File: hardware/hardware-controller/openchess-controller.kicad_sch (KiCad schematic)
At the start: 24 parts, among them J1 Conn_02x13, J2 USB_C_Receptacle_USB2.0_16P, J3 Conn_01x10, U1 AP2112K-3.3, U2 ESP32-DevKitC, U3 74AHCT125

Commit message: Add new mechanical and power symbols for schematic integration
- Introduced new symbols: TestPoint, Fiducial, MountingHole, +3V3, and GND.
- Each symbol includes properties for reference, value, footprint, datasheet, description, keywords, and filters.
- Implemented a Python script to merge test/mech snippets into the main schematic, ensuring backup and validation of parens.
- The script adds missing symbol definitions and integrates component instances, labels, wires, and power ports.
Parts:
- removed C3, C4: 1µF, symbol Device:C
- removed J2: USB_C_Receptacle_USB2.0_16P, Connector_USB:USB_C_Receptacle_GCT_USB4085, symbol Connector:USB_C_Receptacle_USB2.0_16P
- removed R10, R9: 5.1k, symbol Device:R
- removed U1: AP2112K-3.3, Package_TO_SOT_SMD:SOT-23-5, symbol Regulator_Linear:AP2112K-3.3
- added BT1: LiPo 1S 3.7V (protected), symbol Device:Battery_Cell
- added C11, C12: 100nF, Capacitor_SMD:C_0603_1608Metric, symbol Device:C
- added D2: SS14 (or BAT60A), Diode_SMD:D_SMA, symbol Device:D_Schottky
- added FID1, FID2, FID3: Fiducial, Fiducial:Fiducial_1mm_Mask2mm, symbol Mechanical:Fiducial
- added M1: Lipo Rider Plus, LipoRiderPlus:MODULE_106990290, symbol Connector_Generic:Conn_01x08
- added MH1, MH2, MH3, MH4: M3, MountingHole:MountingHole_3.2mm_M3, symbol Mechanical:MountingHole
- added R14: 220k, Resistor_SMD:R_0603_1608Metric, symbol Device:R
- added R15: 100k, Resistor_SMD:R_0603_1608Metric, symbol Device:R
- added TP1, TP10, TP11, TP12, TP13, TP14, TP15, TP16, TP17, TP18, TP19, TP2, TP20, TP21, TP22, TP3, TP4, TP5, TP6, TP7, TP8, TP9: TestPoint, TestPoint:TestPoint_Pad_D1.5mm, symbol Connector:TestPoint
- added U6: TBD62783A, Package_DIP:DIP-18_W7.62mm, symbol Transistor_Array:TBD62783A
- C1, C2, C5: footprint (none) -> Capacitor_SMD:C_0805_2012Metric
- J1: footprint (none) -> Connector_PinHeader_2.54mm:PinHeader_2x13_P2.54mm_Vertical
- J3: value Conn_01x10 -> J_PANEL XH-10
- R1, R2, R3, R4, R5, R6, R7, R8: footprint (none) -> Resistor_SMD:R_0805_2012Metric
- R11: value R -> 33Ω; footprint (none) -> Resistor_SMD:R_0603_1608Metric
- R36, R37: footprint (none) -> Resistor_SMD:R_0603_1608Metric
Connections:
- net +3.3V: now also M1.1 (Pin_1), TP2.1
- net +5V_LED: now also U3.14 (VCC), C11.1, D2.2 (A), M1.4 (Pin_4), TP1.1, U6.9 (VCC)
- net CA_PWR: now also TP15.1, U6.18 (O1)
- net CB_PWR: now also TP16.1, U6.17 (O2)
- net CC_PWR: now also TP17.1, U6.16 (O3)
- net CD_PWR: now also TP18.1, U6.15 (O4)
- net CE_PWR: now also TP19.1, U6.14 (O5)
- net CF_PWR: now also TP20.1, U6.13 (O6)
- net CG_PWR: now also TP21.1, U6.12 (O7)
- net CH_PWR: now also TP22.1, U6.11 (O8)
- net COL_DRV_A: now also U6.1 (I1)
- net COL_DRV_B: now also U6.2 (I2)
- net COL_DRV_C: now also U6.3 (I3)
- net COL_DRV_D: now also U6.4 (I4)
- net COL_DRV_E: now also U6.5 (I5)
- net COL_DRV_F: now also U6.6 (I6)
- net COL_DRV_G: now also U6.7 (I7)
- net COL_DRV_H: now also U6.8 (I8)
- net GND: now also U3.7 (GND), C11.2, C12.2, M1.3 (Pin_3), M1.5 (Pin_5), M1.7 (Pin_7), R15.2, TP3.1, U6.10 (GND)
- net LED_DATA: now also TP4.1
- net LED_DATA_5V: now also TP5.1
- net PANEL_SPARE: now also J3.8 (Pin_8); no longer J3.9 (Pin_9)
- net S0: now also TP7.1; no longer U2.27 (GPIO16)
- net S1: now also U2.27 (GPIO16), TP8.1
- net S2: now also TP9.1
- net S3: now also TP10.1
- net S4: now also TP11.1
- net S5: now also TP12.1
- net S6: now also TP13.1
- net S7: now also TP14.1
- net at U2.19 (5V): now also D2.1 (K)
- net VBAT_MON: now reaches U2.5 (VDET_1/GPIO34/ADC1_CH6)
- net VBAT_MON: now also C12.1, R14.2, R15.1, TP6.1
- net BTN_RESET: no longer names the net of U2.2 (CHIP_PU)
- net BTN_RESET: no longer J3.8 (Pin_8)
- net LED_BATT_N renamed BTN_SELECT
- net LED_CONN_N renamed I2C_SCL
- net LED_PWR_N renamed I2C_SDA
- new net BAT: M1.6 (Pin_6), R14.1
- new net PANEL_SPARE2: J3.9 (Pin_9)
- no-connect marks 20 -> 17
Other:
- note added: "J3 JST XH 10-pin / → OLED + 3 panel-mount buttons / via flying-lead harness (no panel PCB)"
- note added: "M1 Lipo Rider Plus (USB-C) / → +5V_LED + +3V3 rails / LiPo battery via M1 JST / D2 Schottky → DevKit pin 19"
- note added: "R1..R8 — 10k S0..S7 pulled to +3.3V on controller Hall outputs are open-collector"
- note added: "U2 ESP32-DevKitC v4 / UART0 (GPIO1/3) repurposed as I²C / Flash pins + extras → NC"
- note added: "U3 74AHCT125 quad buffer / Gate A active, B/C/D tied off / R11 33Ω series on output"
- note added: "U6 TBD62783A 8-channel / high-side P-MOSFET driver IC / COL_DRV_A..H → CA..CH_PWR"
- note removed: "CA_PWR..CH_PWR switched 5V column rails Implementation pending: direct GPIO vs 74HC595 + transistors"
- note removed: "Cable-mounted side controls Status LEDs and buttons live off-board Pinout pending"
- note removed: "ESP32 data -> 5V WS2812 data Target net: LED_DATA_5V Part choice pending"
- note removed: "ESP32 module/devkit placeholder GPIO assignment to be locked before placement +3V3 logic rail"
- note removed: "R1..R8 — 10k S0..S7 pulled to +3V3 on controller Hall outputs are open-collector"
- note removed: "USB-C 5V → +5V_LED rail +3V3 LDO (AP2112K-3.3, 600 mA) No battery on prototype #1"
- moved on the sheet: C1, C2, C5, J3, R11, R36, R37, U2, U3A, U3B, U3C, U3D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

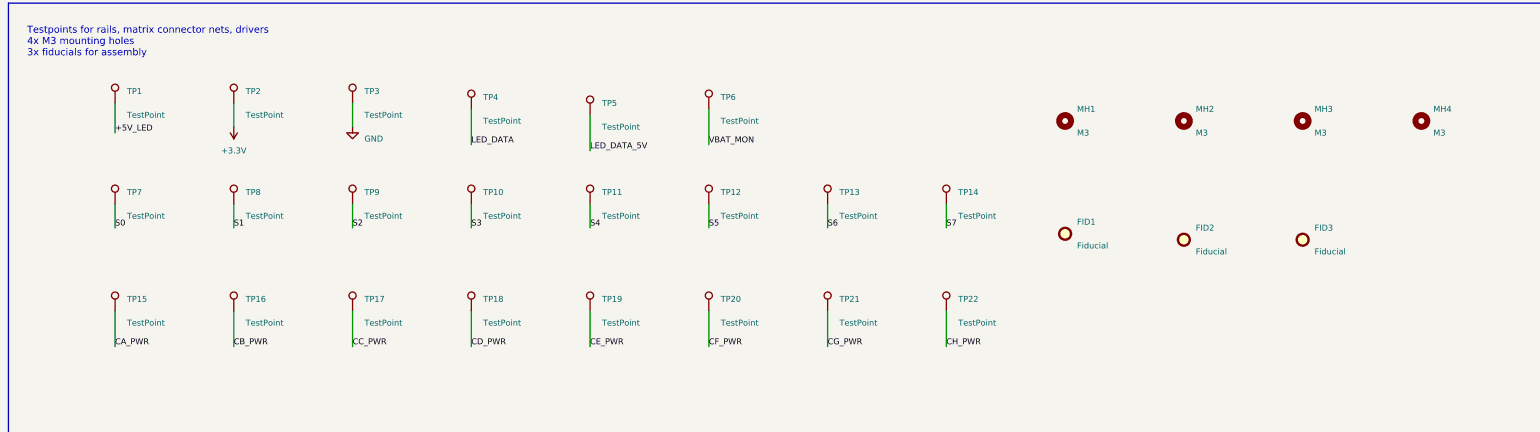
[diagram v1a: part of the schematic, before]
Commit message: Add PCB layout and schematic guides for OpenChess controller
- Introduced `controller-PCB_LAYOUT_GUIDE.planning.md` detailing PCB layout constraints, component placement zones, net classes, routing priorities, and mechanical verification for the OpenChess controller.
- Added `controller-SCHEMATIC_GUIDE.planning.md` providing a comprehensive schematic specification, including reference designators, net lists, component details, and validation rules for the OpenChess controller PCB.
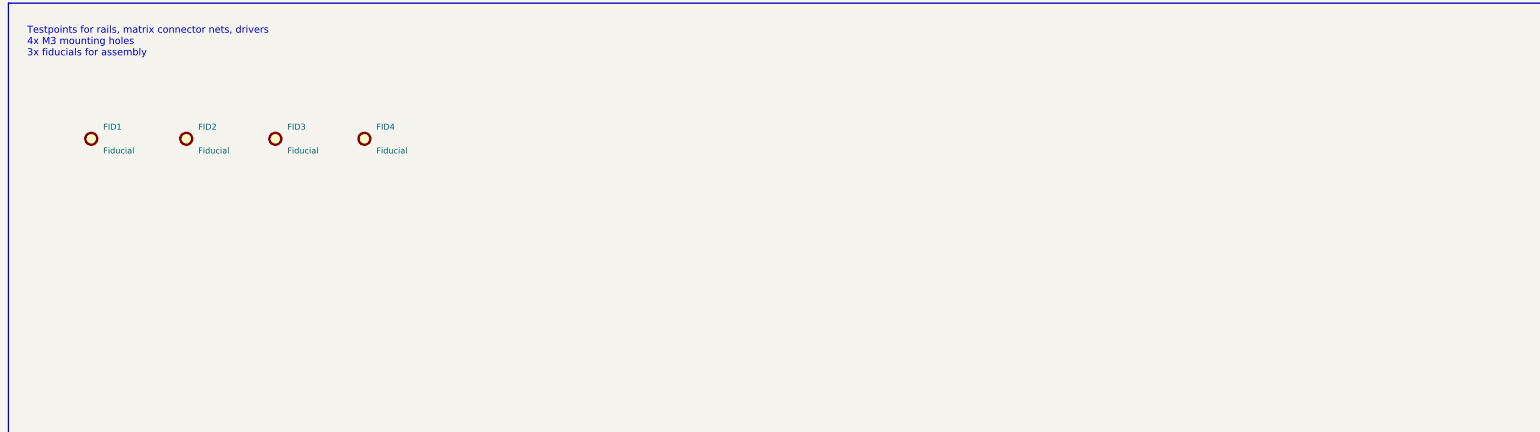
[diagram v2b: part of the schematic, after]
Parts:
- removed MH1, MH2, MH3, MH4: M3, MountingHole:MountingHole_3.2mm_M3, symbol Mechanical:MountingHole
- removed TP1, TP10, TP11, TP12, TP13, TP14, TP15, TP16, TP17, TP18, TP19, TP2, TP20, TP21, TP22, TP3, TP4, TP5, TP6, TP7, TP8, TP9: TestPoint, TestPoint:TestPoint_Pad_D1.5mm, symbol Connector:TestPoint
- added FID4: Fiducial, Fiducial:Fiducial_1mm_Mask2mm, symbol Mechanical:Fiducial
- J3: footprint Connector_PinHeader_2.54mm:PinHeader_1x10_P2.54mm_Horizontal -> Connector_PinHeader_2.54mm:PinHeader_1x10_P2.54mm_Vertical
- M1: footprint LipoRiderPlus:MODULE_106990290 -> Connector_PinSocket_2.54mm:PinSocket_1x08_P2.54mm_Vertical
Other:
- moved on the sheet: FID1, FID2
